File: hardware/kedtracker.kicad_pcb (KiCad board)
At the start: 2 copper layers, 82.7 x 56.6 mm, 80 parts, among them J1 ANT, J2 SWD, J3 BOOT, J4 IGC, J5 Micro USB, J6 BT_KEY, J7 UART, J8 VK2828U7G5LF, J9 Micro SD Reader, SW1 RESET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

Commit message: Prepare fabrication layer for assembly
* Proper placement of labels on F.Fab layer
* Element outlines
* Correct values of used components
* LED values indicate color, rather then function
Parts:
- D1: value 1N4001 -> SS14
- F1: value 0.5A -> 0.2A
- J9: value Micro SD Reader -> SDCARD_READER
- LED1: value STATUS_PANEL -> GREEN
- LED2: value STATUS_SMD -> YELLOW
- LED3: value LED_BT -> BLUE
- LED4: value LED_BT_STATUS -> BLUE
- LED5: value PWR -> RED
- LS1: value Buzzer -> BUZZER
- R1: value 82 -> 100
- R2, R3: value 330 -> 520
- R7: value 82 -> 820
- U1: value LM2936-3.3 -> LM3940
- Y2: value 8MHz -> 8M

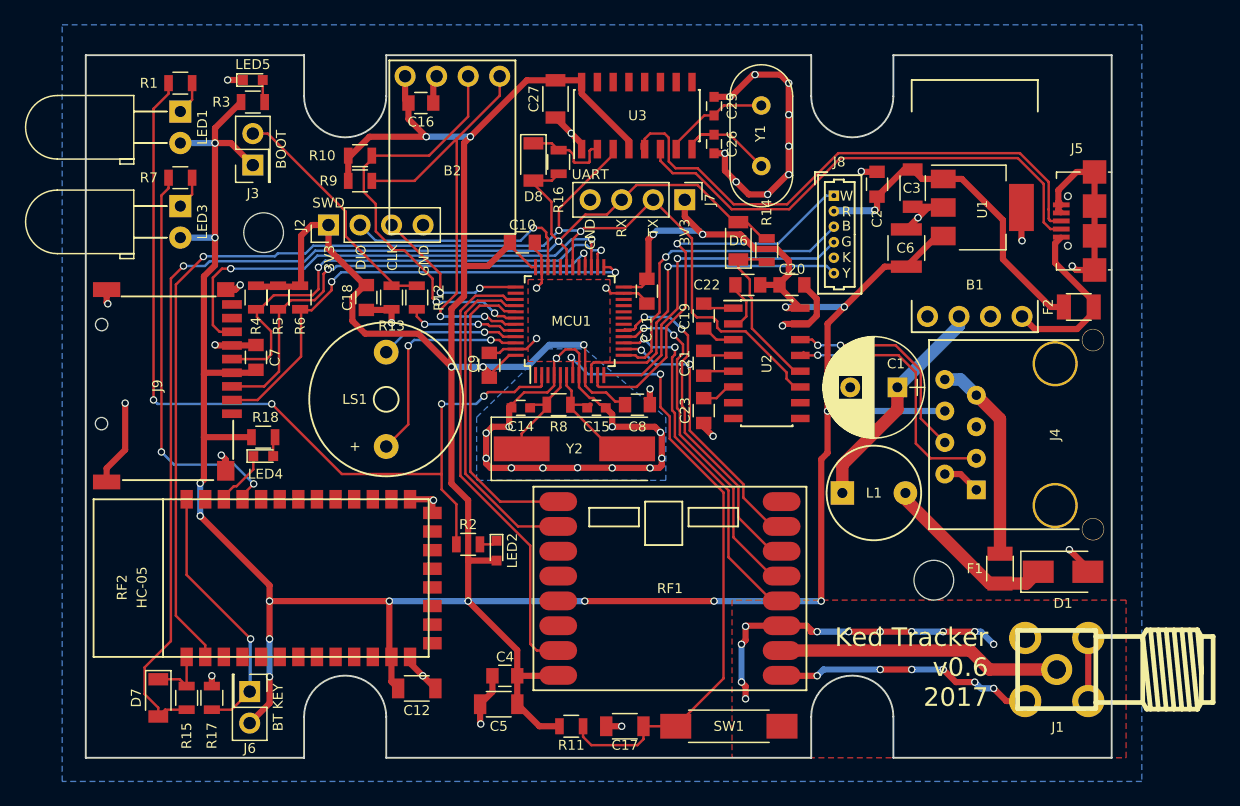
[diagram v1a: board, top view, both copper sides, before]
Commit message: Changes and fixes for 0.7
* Different 4-pin reset button (because I have a lot of those)
* Bluethooth "paired" and "status" leds swapped - dashboard
  led will show "paired" status and will not annoyingly blink all
  the time
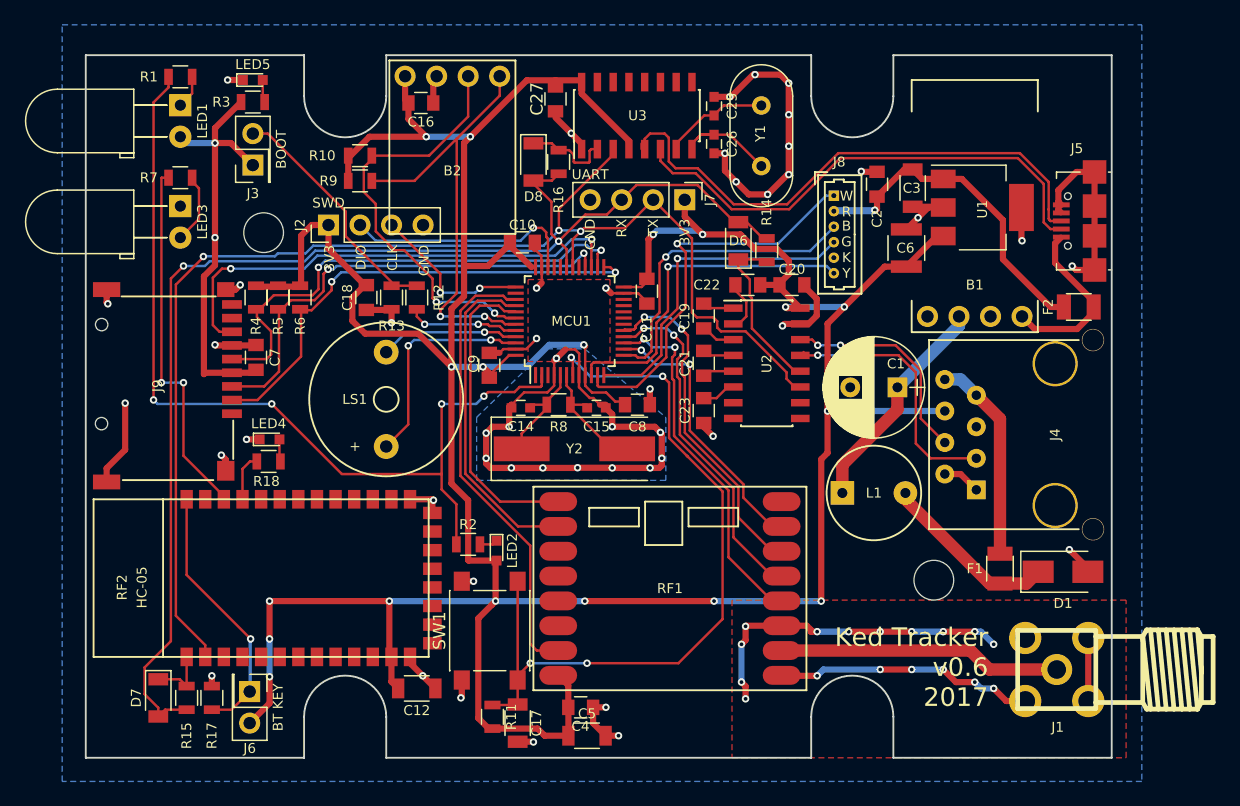
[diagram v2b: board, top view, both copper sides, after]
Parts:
- C27: footprint Capacitors_SMD:C_1206 -> Capacitors_SMD:C_0805
- R17: value 100K -> 10K
- SW1: footprint Buttons_Switches_SMD:SW_SPST_REED_CT05-XXXX-G1 -> Buttons_Switches_SMD:SW_SPST_PTS645
- moved SW1 20.8 mm to (132.5, 89.8), turned to 90 degrees
- moved C17 8.64 mm to (134.8, 97.2), turned to 270 degrees
- moved C5 7.55 mm to (140.4, 98.2), turned to 0 degrees
- moved C4 6.62 mm to (139.9, 95.9), turned to 0 degrees
- moved R11 6.40 mm to (132.8, 96.7), turned to 90 degrees
- moved R18 2.00 mm to (114.7, 76.1), turned to 180 degrees
- moved LED4 1.44 mm to (114.8, 74.3)
- moved LED1 0.51 mm to (107.6, 47.4)
- moved R1 0.51 mm to (107.6, 45.1)
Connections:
- LED3 pad 1: Net-(LED3-Pad1) -> Earth
- LED3 pad 2: 3.3V -> Net-(LED3-Pad2)
- LED4 pad 1: /Console/BT_STATUS -> Earth
- R18 pad 1: 3.3V -> Net-(LED4-Pad2)
- R18 pad 2: Net-(LED4-Pad2) -> /Console/BT_STATUS
- R7 pad 2: Net-(LED3-Pad1) -> Net-(LED3-Pad2)
- RF2 pad 31: /Console/BT_PAIRED -> /Console/BT_STATUS
- RF2 pad 32: /Console/BT_STATUS -> /Console/BT_PAIRED
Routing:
- net 3.3V: track 356.0 -> 334.6 mm, vias 22 -> 20
- net /RESET: track 51.1 -> 61.9 mm, vias 2 -> 4
- net Net-(LED3-Pad2): track 0.00 -> 5.68 mm
- net Earth: track 167.1 -> 171.4 mm, vias 50 -> 54
- net Net-(LED3-Pad1): track 3.13 -> 0.00 mm
- net /Console/BT_PAIRED: track 32.4 -> 29.6 mm
- net /STAT_LED: track 73.0 -> 73.6 mm
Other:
- net class ANT: via_drill 0.4 -> 0.3
- net class Default: via_drill 0.4 -> 0.3
- net class HV: via_drill 0.4 -> 0.3
- net class PWR: via_drill 0.4 -> 0.3

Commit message: Baro board turned 90 degrees to fit into the board
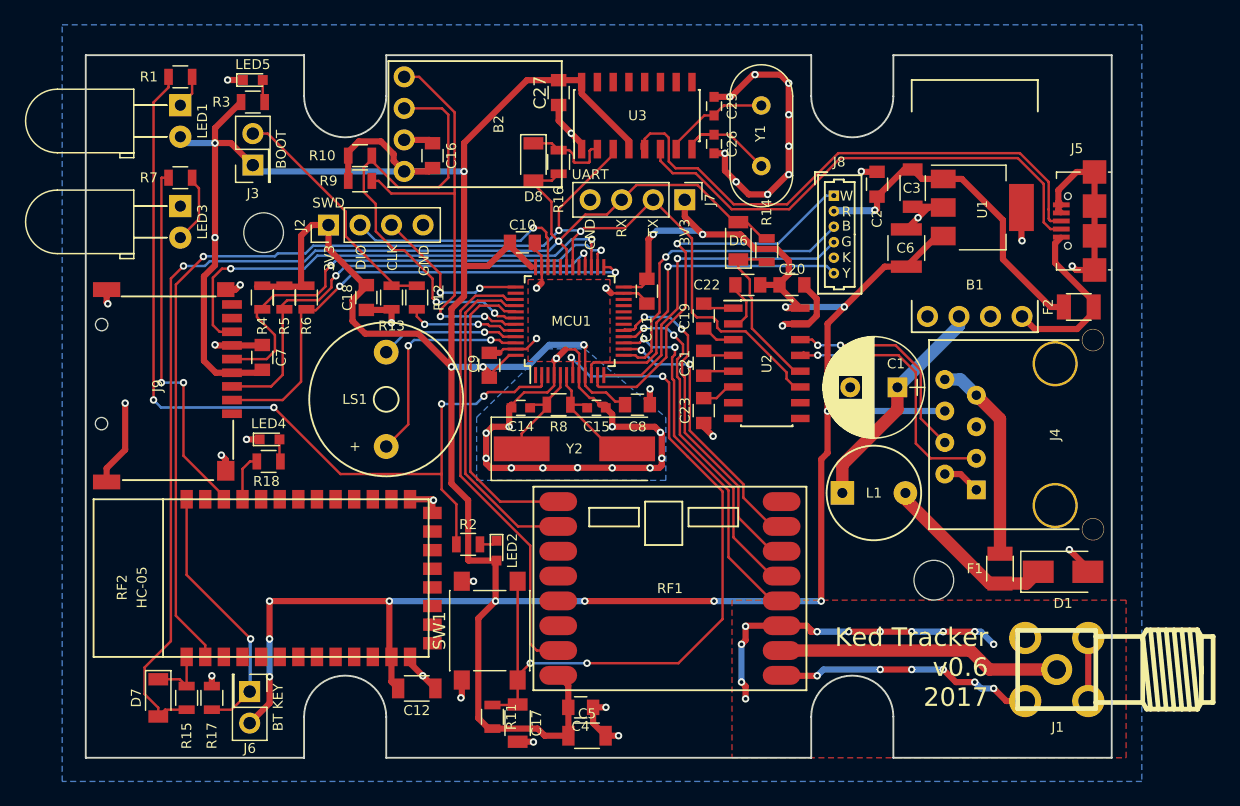
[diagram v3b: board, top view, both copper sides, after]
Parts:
- moved C16 4.34 mm to (127.9, 51.5), turned to 90 degrees
- moved B2 1.89 mm to (128.2, 48.9), turned to 270 degrees
- moved C27 0.57 mm to (138.1, 46.4)
- moved C7 0.51 mm to (114.2, 67.7)
- moved R4 0.51 mm to (114.2, 62.9)
- moved R5 0.51 mm to (116.0, 62.9)
- moved R6 0.51 mm to (117.8, 62.9)
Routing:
- net 3.3V: track 334.6 -> 343.9 mm, vias 20 -> 19
- net /BARO_SCL: track 34.2 -> 38.9 mm
- net Earth: track 171.4 -> 172.5 mm
- net /SD_CS: track 38.6 -> 39.4 mm

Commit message: Updates for power supply and reset button
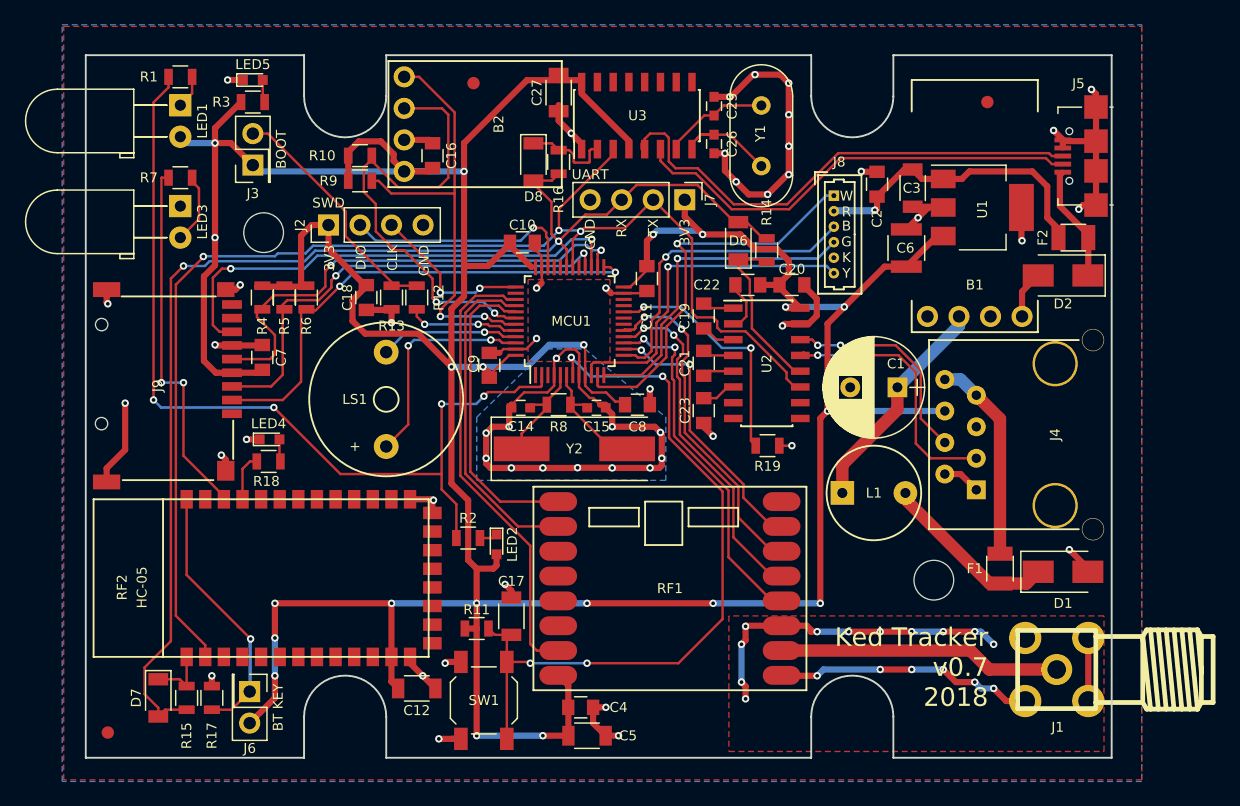
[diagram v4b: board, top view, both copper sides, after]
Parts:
- added D2: SS14, Diodes_SMD:D_SMA_Standard, F.Cu at (178.7, 61.1)
- added R19: 10K, Resistors_SMD:R_0805, F.Cu at (154.9, 74.9)
- added REF**: Fiducial_1mm_Dia_2.54mm_Outer_CopperTop, Fiducials:Fiducial_1mm_Dia_2.54mm_Outer_CopperTop, F.Cu at (131.2, 45.6)
- added REF**: Fiducial_1mm_Dia_2.54mm_Outer_CopperTop, Fiducials:Fiducial_1mm_Dia_2.54mm_Outer_CopperTop, F.Cu at (172.6, 47.2)
- added REF**: Fiducial_1mm_Dia_2.54mm_Outer_CopperTop, Fiducials:Fiducial_1mm_Dia_2.54mm_Outer_CopperTop, F.Cu at (101.8, 98.0)
- C27: footprint Capacitors_SMD:C_0805 -> Capacitors_SMD:C_1206
- SW1: footprint Buttons_Switches_SMD:SW_SPST_PTS645 -> Buttons_Switches_SMD:SW_SPST_SKQG
- moved C17 8.63 mm to (134.3, 88.6), turned to 90 degrees
- moved R11 7.22 mm to (131.5, 89.6), turned to 0 degrees
- moved SW1 5.64 mm to (132.1, 95.4)
- moved F2 5.61 mm to (179.6, 58.1)
- moved J5 5.23 mm to (180.0, 51.5)
- moved C11 1.02 mm to (145.2, 61.4)
- moved LED2 0.51 mm to (133.1, 82.8)
- moved R2 0.51 mm to (130.8, 82.3)
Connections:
- B1 pad 4: 5V -> /5V_OUT
- MCU1 pad 20: (no net) -> /BOOT1
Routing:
- net /BOOT1: track 0.00 -> 19.8 mm, vias 0 -> 2
- net 5V: track 14.3 -> 9.32 mm
- net /Console/CON_USB_D-: track 40.7 -> 36.9 mm
- net /5V_OUT: track 0.00 -> 3.84 mm
- net /Console/CON_USB_D+: track 44.2 -> 40.4 mm
- net /5V_PROT: track 30.2 -> 27.7 mm
- net Earth: track 172.5 -> 174.9 mm, vias 54 -> 57
- net /RESET: track 61.8 -> 60.3 mm
- net 3.3V: track 343.9 -> 344.8 mm, vias 19 -> 21
- net /STAT_LED: track 73.6 -> 73.0 mm
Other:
- net class ANT: clearance 0.3 -> 0.2
- board text added: "Ked Tracker v0.7"
- board text added: "Ked Tracker v0.7 2018"
- board text removed: "Ked Tracker v0.6"
- board text removed: "Ked Tracker v0.6 2017"

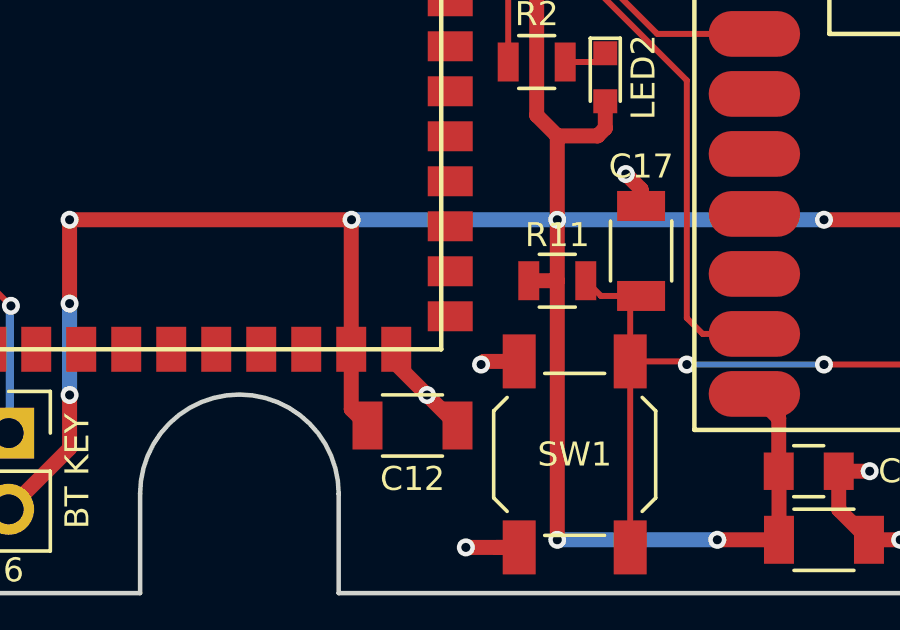
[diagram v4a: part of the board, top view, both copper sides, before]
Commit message: Reset button resets bluetooth chip as well
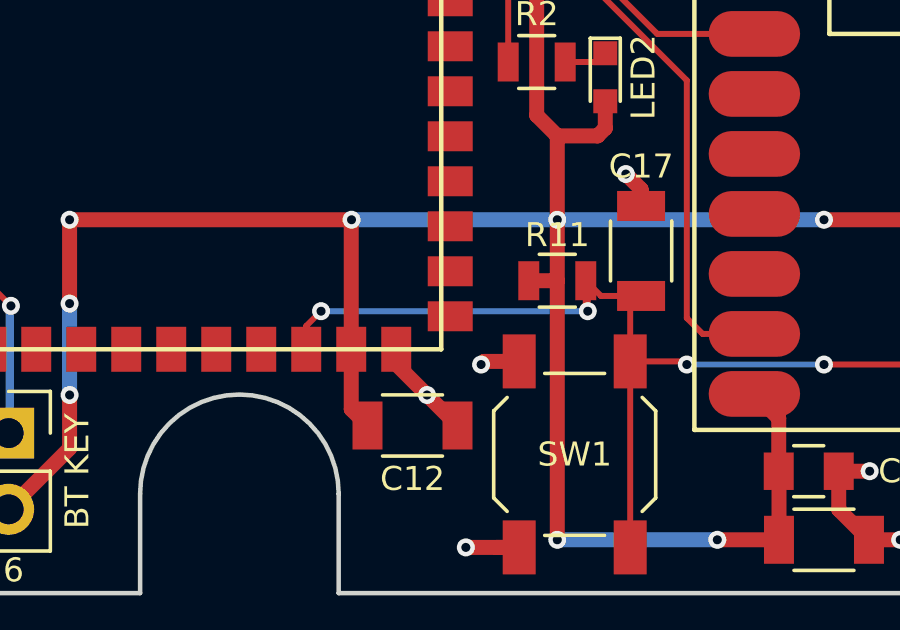
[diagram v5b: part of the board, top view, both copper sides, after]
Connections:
- RF2 pad 11: (no net) -> /RESET
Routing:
- net /RESET: track 60.3 -> 72.2 mm, vias 4 -> 6
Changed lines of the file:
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@@
 (kicad_pcb (version 4) (host pcbnew 4.0.6+dfsg1-1)
   (general
-    (links 0)
-    (no_connects 0)
+    (links 204)
+    (no_connects 1)
     (area 99.924999 43.314999 182.735001 100.075001)
     (thickness 1.6)
     (drawings 49)
-    (tracks 1027)
+    (tracks 1036)
     (zones 0)
     (modules 85)
@@
     (pad 9 smd rect (at 0 -6 90) (size 1.5 1) (layers F.Cu F.Paste F.Mask))
     (pad 10 smd rect (at 0 -4.5 90) (size 1.5 1) (layers F.Cu F.Paste F.Mask))
-    (pad 11 smd rect (at 0 -3 90) (size 1.5 1) (layers F.Cu F.Paste F.Mask))
+    (pad 11 smd rect (at 0 -3 90) (size 1.5 1) (layers F.Cu F.Paste F.Mask)
+      (net 36 /RESET))
     (pad 12 smd rect (at 0 -1.5 90) (size 1.5 1) (layers F.Cu F.Paste F.Mask)
       (net 1 3.3V))
@@
   (segment (start 143.62 74.854) (end 142.37 74.854) (width 0.2) (layer F.Cu) (net 35) (status 30))
   (segment (start 140.64 71.552) (end 140.665 71.552) (width 0.2) (layer F.Cu) (net 35) (status 30))
+  (segment (start 132.512 90.177736) (end 132.512 90.602) (width 0.2) (layer F.Cu) (net 36))
+  (segment (start 132.446 90.536) (end 132.512 90.602) (width 0.2) (layer F.Cu) (net 36))
+  (segment (start 132.446 89.586) (end 132.446 90.536) (width 0.2) (layer F.Cu) (net 36))
+  (segment (start 132.512 90.16) (end 132.512 90.177736) (width 0.2) (layer F.Cu) (net 36))
+  (via (at 132.512 90.602) (size 0.6) (drill 0.3) (layers F.Cu B.Cu) (net 36))
+  (segment (start 123.622 90.602) (end 132.512 90.602) (width 0.2) (layer B.Cu) (net 36))
+  (segment (start 123.128 91.872) (end 123.128 91.096) (width 0.2) (layer F.Cu) (net 36))
+  (segment (start 123.128 91.096) (end 123.622 90.602) (width 0.2) (layer F.Cu) (net 36))
+  (via (at 123.622 90.602) (size 0.6) (drill 0.3) (layers F.Cu B.Cu) (net 36))
   (segment (start 134.29 90.094) (end 132.954 90.094) (width 0.2) (layer F.Cu) (net 36) (status 10))
   (segment (start 132.954 90.094) (end 132.446 89.586) (width 0.2) (layer F.Cu) (net 36) (status 20))

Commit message: Preparing release 0.7
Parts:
- added REF**: Fiducial_1mm_Dia_2.54mm_Outer_CopperTop, Fiducials:Fiducial_1mm_Dia_2.54mm_Outer_CopperTop, F.Cu at (148.3, 97.5)
- C1: footprint Capacitors_ThroughHole:CP_Radial_D8.0mm_P3.80mm -> Capacitors_ThroughHole:CP_Radial_D6.3mm_P2.50mm
- C27: footprint Capacitors_SMD:C_1206 -> Capacitors_SMD:C_0805
- moved REF** 9.32 mm to (133.0, 54.8)
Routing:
- net /CON1_TXD: track 106.1 -> 107.3 mm
- net /CON1_RXD: track 102.5 -> 103.5 mm
- net /SD_MISO: track 39.7 -> 40.5 mm
- net /SUP_PROT: track 14.4 -> 15.0 mm
